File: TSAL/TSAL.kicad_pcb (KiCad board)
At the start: 2 copper layers, 100.2 x 100.2 mm, 65 parts, among them J1 Screw_Terminal_01x02, J2 Screw_Terminal_01x02, K1 RELAY_19.1x15.5mm, Q1 BC548, Q2 IRF3205, Q3 IRF3205, U1 MC34063AP, U2 TLP290-4, U3 LM555, U4 TL431DBZ, U5 TL431DBZ, U6 LM358

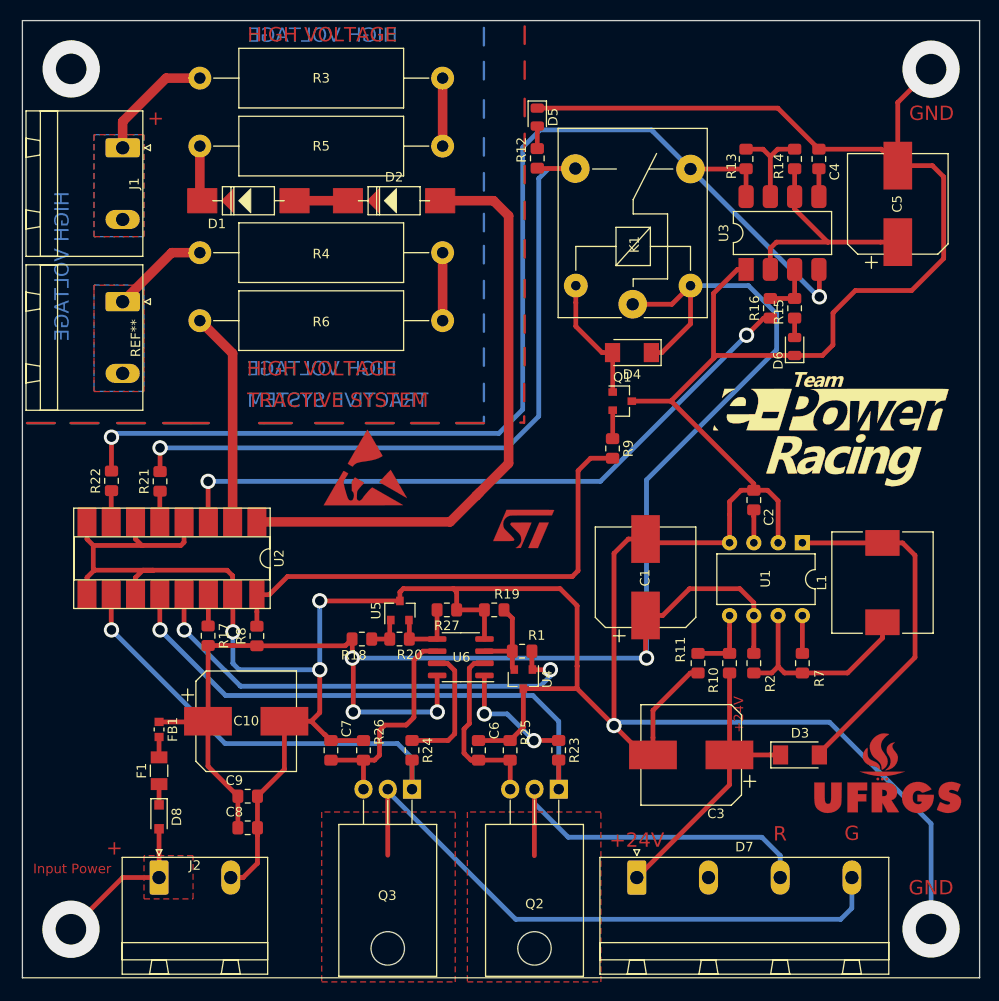
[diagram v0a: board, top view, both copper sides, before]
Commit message: TSAL rounded corners
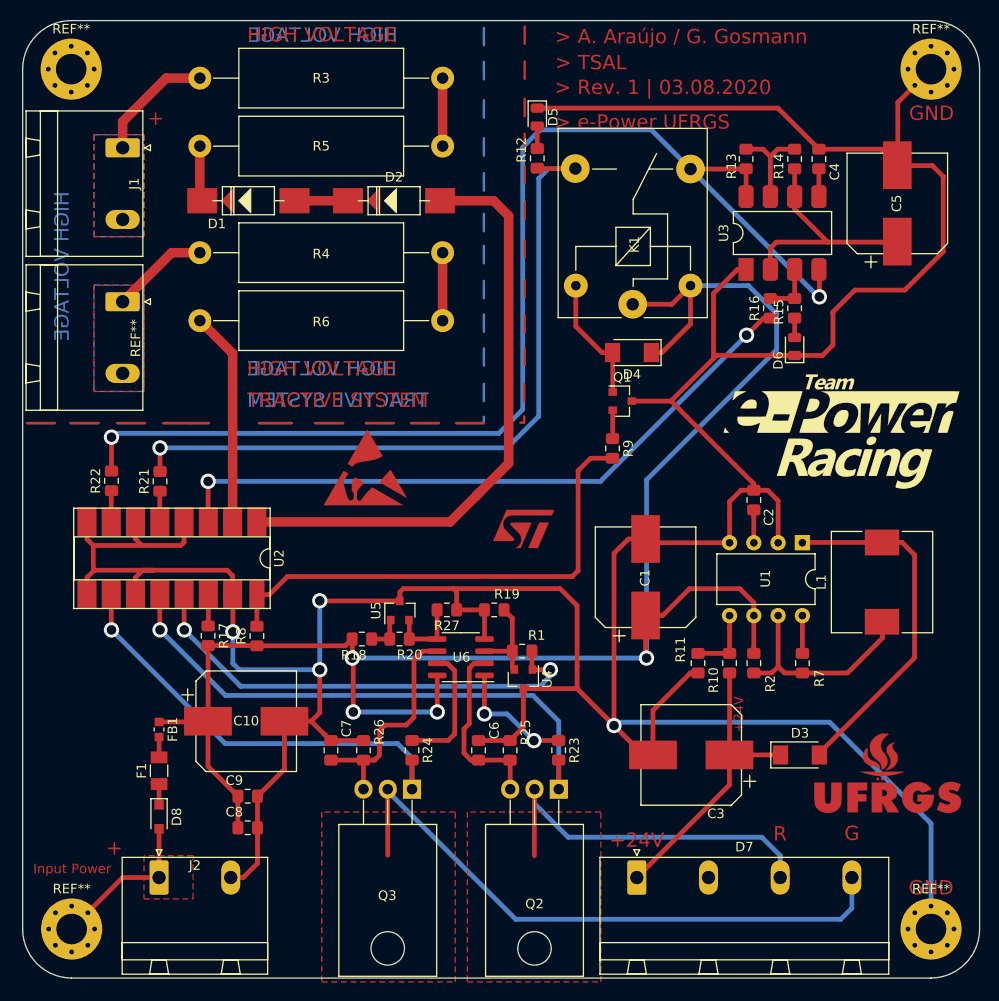
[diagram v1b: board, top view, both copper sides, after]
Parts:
- added REF**: MountingHole_3.2mm_M3_Pad_Via, e-Power:MountingHole_3.2mm_M3_Pad_Via, F.Cu at (133.9, 145.6)
- added REF**: MountingHole_3.2mm_M3_Pad_Via, e-Power:MountingHole_3.2mm_M3_Pad_Via, F.Cu at (223.8, 145.6)
- added REF**: MountingHole_3.2mm_M3_Pad_Via, e-Power:MountingHole_3.2mm_M3_Pad_Via, F.Cu at (223.8, 55.6)
- added REF**: MountingHole_3.2mm_M3_Pad_Via, e-Power:MountingHole_3.2mm_M3_Pad_Via, F.Cu at (133.8, 55.6)
- moved G*** 1.15 mm to (214.4, 93.5)
- moved C5 0.07 mm to (220.2, 69.7)
- moved L1 0.07 mm to (218.6, 109.3)
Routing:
- net GND: track 409.2 -> 408.8 mm, vias 6 -> 4
- net Input_Power: vias 1 -> 0
- net (no net): vias 1 -> 0
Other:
- board size 100.2 x 100.2 mm -> 100.1 x 100.2 mm
- board text added: "> A. Araújo / G. Gosmann"
- board text added: "> Rev. 1 | 03.08.2020"
- board text added: "> TSAL"
- board text added: "> e-Power UFRGS"

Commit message: update all circuits
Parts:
- removed the C1 at (193.9, 108.8)
- removed the C6 at (176.4, 126.9)
- removed the D3 at (210.1, 127.4)
- removed the D4 at (192.5, 85.3)
- removed G***: LOGO, e-Power:e-Power_22.8x12.0mm_Copper
- removed G***: LOGO, e-Power:ST_6.5x4.1mm_Copper
- removed G***: LOGO, e-Power:UFRGS_14.7x8.0mm_Copper
- removed the R10 at (202.7, 117.8)
- removed the R14 at (209.5, 65.0)
- removed REF** (x4): MountingHole_3.2mm_M3_Pad_Via, e-Power:MountingHole_3.2mm_M3_Pad_Via
- removed REF**: ESD-Logo_8.9x8mm_Copper, e-Power:ESD-Logo_8.9x8mm_Copper
- removed REF**: PhoenixContact_GMSTBA_2,5_2-G_1x02_P7.50mm_Horizontal, Connector_Phoenix_GMSTB:PhoenixContact_GMSTBA_2,5_2-G_1x02_P7.50mm_Horizontal
- removed the U4 at (181.1, 119.4)
- removed the U5 at (168.2, 112.3)
- added C11: 100nF, Capacitor_SMD:C_0805_2012Metric_Pad1.15x1.40mm_HandSolder, F.Cu at (183.7, 95.0)
- added C12: 100nF, Capacitor_SMD:C_0805_2012Metric_Pad1.15x1.40mm_HandSolder, F.Cu at (217.6, 86.2)
- added C13: 100nF, Capacitor_SMD:C_0805_2012Metric_Pad1.15x1.40mm_HandSolder, F.Cu at (220.6, 86.2)
- added C4: 100nF, Capacitor_SMD:C_0805_2012Metric_Pad1.15x1.40mm_HandSolder, F.Cu at (192.2, 87.8)
- added C5: 220u, e-Power:CP_Elec_10x10, F.Cu at (167.1, 92.3)
- added D2: SS54HF, e-Power:DO-214AC, F.Cu at (186.2, 88.4)
- added D7: SS54HF, e-Power:DO-214AC, F.Cu at (177.7, 94.9)
- added H1: MountingHole_Pad, e-Power:MountingHole_3.2mm_M3_Pad_Via, F.Cu at (134.3, 146.1)
- added H2: MountingHole_Pad, e-Power:MountingHole_3.2mm_M3_Pad_Via, F.Cu at (215.6, 130.7)
- added H3: MountingHole_Pad, e-Power:MountingHole_3.2mm_M3_Pad_Via, F.Cu at (223.5, 122.8)
- added H4: MountingHole_Pad, e-Power:MountingHole_3.2mm_M3_Pad_Via, F.Cu at (223.5, 130.7)
- added R12: 100K, Resistor_SMD:R_0805_2012Metric_Pad1.15x1.40mm_HandSolder, F.Cu at (181.3, 98.5)
- added R13: 100K, Resistor_SMD:R_0805_2012Metric_Pad1.15x1.40mm_HandSolder, F.Cu at (176.5, 98.5)
- added R17: 1R, Resistor_SMD:R_0805_2012Metric_Pad1.15x1.40mm_HandSolder, F.Cu at (185.0, 92.0)
- added R18: 10R, Resistor_SMD:R_0805_2012Metric_Pad1.15x1.40mm_HandSolder, F.Cu at (189.7, 92.0)
- added R19: 10R, Resistor_SMD:R_0805_2012Metric_Pad1.15x1.40mm_HandSolder, F.Cu at (176.5, 104.3)
- added R20: 10R, Resistor_SMD:R_0805_2012Metric_Pad1.15x1.40mm_HandSolder, F.Cu at (181.3, 101.4)
- added R24: 10K, Resistor_SMD:R_0805_2012Metric_Pad1.15x1.40mm_HandSolder, F.Cu at (196.9, 87.8)
- added R27: 10R, Resistor_SMD:R_0805_2012Metric_Pad1.15x1.40mm_HandSolder, F.Cu at (186.0, 97.9)
- added R28: 10R, Resistor_SMD:R_0805_2012Metric_Pad1.15x1.40mm_HandSolder, F.Cu at (194.5, 90.8)
- added R31: 10K, Resistor_SMD:R_0805_2012Metric_Pad1.15x1.40mm_HandSolder, F.Cu at (176.5, 101.4)
- added R32: 100K, Resistor_SMD:R_0805_2012Metric_Pad1.15x1.40mm_HandSolder, F.Cu at (186.0, 100.8)
- added R33: 10R, Resistor_SMD:R_0805_2012Metric_Pad1.15x1.40mm_HandSolder, F.Cu at (181.3, 107.3)
- added R34: 10R, Resistor_SMD:R_0805_2012Metric_Pad1.15x1.40mm_HandSolder, F.Cu at (194.5, 93.7)
- added R35: 10R, Resistor_SMD:R_0805_2012Metric_Pad1.15x1.40mm_HandSolder, F.Cu at (190.8, 97.9)
- added R39: 10R, Resistor_SMD:R_0805_2012Metric_Pad1.15x1.40mm_HandSolder, F.Cu at (199.2, 90.8)
- added R40: 10R, Resistor_SMD:R_0805_2012Metric_Pad1.15x1.40mm_HandSolder, F.Cu at (186.0, 103.8)
- added R41: 10R, Resistor_SMD:R_0805_2012Metric_Pad1.15x1.40mm_HandSolder, F.Cu at (190.8, 100.8)
- added R43: 10R, Resistor_SMD:R_0805_2012Metric_Pad1.15x1.40mm_HandSolder, F.Cu at (181.3, 104.3)
- added R44: 10R, Resistor_SMD:R_0805_2012Metric_Pad1.15x1.40mm_HandSolder, F.Cu at (186.0, 106.8)
- added R45: 10R, Resistor_SMD:R_0805_2012Metric_Pad1.15x1.40mm_HandSolder, F.Cu at (199.2, 93.7)
- added R46: 10R, Resistor_SMD:R_0805_2012Metric_Pad1.15x1.40mm_HandSolder, F.Cu at (195.5, 96.7)
- added R47: 10R, Resistor_SMD:R_0805_2012Metric_Pad1.15x1.40mm_HandSolder, F.Cu at (190.8, 103.8)
- added R48: 10R, Resistor_SMD:R_0805_2012Metric_Pad1.15x1.40mm_HandSolder, F.Cu at (195.5, 99.6)
- added R49: 10K, Resistor_SMD:R_0805_2012Metric_Pad1.15x1.40mm_HandSolder, F.Cu at (217.6, 81.4)
- added R50: 10K, Resistor_SMD:R_0805_2012Metric_Pad1.15x1.40mm_HandSolder, F.Cu at (223.5, 86.2)
- added TP1: 24V, e-Power:TestPoint_Pad_D1.0mm, F.Cu at (208.3, 129.0)
- added TP2: OUT, e-Power:TestPoint_Pad_D1.0mm, F.Cu at (217.7, 77.5)
- added TP3: Vref_R, e-Power:TestPoint_Pad_D1.0mm, F.Cu at (220.7, 77.8)
- added TP4: RS_R, e-Power:TestPoint_Pad_D1.0mm, F.Cu at (217.7, 74.5)
- added TP5: Vref_G, e-Power:TestPoint_Pad_D1.0mm, F.Cu at (200.8, 99.4)
- added TP6: RS_G, e-Power:TestPoint_Pad_D1.0mm, F.Cu at (220.7, 74.8)
- added TP7: 12V, e-Power:TestPoint_Pad_D1.0mm, F.Cu at (223.8, 74.8)
- added U2: NE555, Package_SO:SOIC-8_3.9x4.9mm_P1.27mm, F.Cu at (178.4, 89.6)
- added U6: TL431DBZ, Package_TO_SOT_SMD:SOT-23, F.Cu at (190.6, 107.5)
- C10: value 470u -> 220u
- C2: renamed from C5; footprint e-Power:CP_Elec_10x10 -> Capacitor_SMD:C_0805_2012Metric
- C3: value 100uF -> 220u
- C8: value 100n -> 100nF
- D4: renamed from D5; value LED -> LED GREEN; footprint LED_SMD:LED_0805_2012Metric -> LED_SMD:LED_0603_1608Metric
- D5: renamed from D6; value LED -> LED RED; footprint LED_SMD:LED_0805_2012Metric -> LED_SMD:LED_0603_1608Metric
- D8: value D_SCH_1N5819 -> SS54HF; footprint Diode_SMD:D_SOD-323_HandSoldering -> e-Power:DO-214AC
- J2: footprint Connector_Phoenix_GMSTB:PhoenixContact_GMSTBA_2,5_2-G_1x02_P7.50mm_Horizontal -> e-Power:TerminalBlock_Phoenix_MKDS-1,5-2_1x02_P5.08mm_Horizontal
- L1: value 170uH -> 100uH; footprint e-Power:L_10.4x10.4_H4.8 -> Inductor_SMD:L_12x12mm_H6mm
- Q1: value BC548 -> Si2302DS
- R14: renamed from R1; value 10K -> 1K
- R16: renamed from R19; value 10K -> ADJ
- R22: renamed from R2; value 0.68R -> 1R
- R25: value 22R -> 100K
- R26: value 27R -> 10R
- R30: renamed from R20; value 10K -> 1K
- R37: renamed from R27; value 10K -> ADJ
- U1: renamed from U2; footprint e-Power:TLP290-4 -> e-Power:SOIC-16_4.55x10.3mm_P1.27mm(TLP290-4)
- U3: value LM555 -> TL431DBZ; footprint Package_DIP:DIP-8_W7.62mm_LongPads -> Package_TO_SOT_SMD:SOT-23
- U5: renamed from U1; footprint Package_DIP:DIP-8_W7.62mm -> Package_SO:SO-8_3.9x4.9mm_P1.27mm
- moved F1 63.9 mm to (203.7, 109.2)
- moved R26 40.0 mm to (188.5, 95.0), turned to 0 degrees
- moved C3 39.2 mm to (167.1, 104.1), turned to 0 degrees
- moved Q1 31.2 mm to (221.4, 81.6), turned to 90 degrees
- moved U3 28.3 mm to (195.4, 103.4), turned to 0 degrees
- moved R25 19.9 mm to (176.5, 107.3), turned to 0 degrees
- moved U5 13.2 mm to (216.4, 93.5)
- moved J2 8.11 mm to (149.0, 145.6)
- renumbered C4 to C1, C2 to C6, D2 to D3, D7 to D6, R3 to R1, R17 to R10, R16 to R11, R23 to R15, R5 to R2, R7 to R23, R18 to R29, R8 to R3, R24 to R36, R11 to R38, R12 to R4, R22 to R42, R9 to R5, R4 to R6, R6 to R7, R13 to R8, R15 to R9, U6 to U4
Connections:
- C1 pad 2: Net-(C4-Pad2) -> Net-(C1-Pad2)
- C2 pad 1: Net-(C5-Pad1) -> Net-(C2-Pad1)
- J1 pad 1: Net-(J1-Pad2) -> Net-(J1-Pad1)
- K1 pad 5: Net-(D4-Pad2) (its old number) -> Net-(D2-Pad2)
- Q1 pad 1: Net-(D4-Pad2) (its old number) -> Net-(Q1-Pad1)
- Q1 pad 2: Net-(Q1-Pad2) -> GND
- Q1 pad 3: GND -> Net-(D2-Pad2)
- Q2 pad 3: Net-(C6-Pad2) (its old number) -> Net-(C4-Pad2)
- R11 pad 2: Net-(R15-Pad2) -> Net-(R11-Pad2)
- R14 pad 1: Net-(R1-Pad1) (its old number) -> Net-(R14-Pad1)
- R14 pad 2: Net-(R1-Pad2) -> Net-(R14-Pad2)
- R16 pad 2: Net-(R1-Pad1) (its old number) -> Net-(R14-Pad1)
- R25 pad 1: GND -> +24V
- R25 pad 2: Net-(C6-Pad2) (its old number) -> Net-(R25-Pad2)
- R26 pad 1: GND -> Net-(R26-Pad1)
- R26 pad 2: Net-(C7-Pad2) -> Net-(R18-Pad1)
- R5 pad 1: Net-(Q1-Pad2) -> Net-(Q1-Pad1)
- R8 pad 2: Net-(R13-Pad2) -> Net-(R12-Pad2)
- R9 pad 2: Net-(R15-Pad2) -> Net-(R11-Pad2)
- U1 pad 13: Net-(R1-Pad2) -> Net-(R14-Pad2)
- U3 pad 1: GND -> Net-(R14-Pad2)
- U3 pad 2: Net-(C5-Pad1) -> Net-(R14-Pad1)
- U3 pad 3: Net-(R15-Pad2) -> GND
- U4 pad 2: Net-(C6-Pad2) (its old number) -> Net-(C12-Pad1)
- U4 pad 3: Net-(R1-Pad1) (its old number) -> Net-(R14-Pad1)
- U4 pad 6: Net-(C7-Pad2) -> Net-(C13-Pad1)
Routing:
- net Net-(R1-Pad2): track 49.4 -> 0.00 mm, vias 2 -> 0
- net Net-(R14-Pad2): track 0.00 -> 49.0 mm, vias 0 -> 2
- net Net-(C6-Pad2) (its old number): track 19.1 -> 0.00 mm
- net Net-(C4-Pad2): track 2.91 -> 19.1 mm
- net Net-(D4-Pad2) (its old number): track 13.4 -> 0.00 mm
- net Net-(D2-Pad2): track 0.00 -> 13.4 mm
- net (no net): track 98.7 -> 88.2 mm, vias 0 -> 2
- net Net-(R13-Pad2): track 9.91 -> 0.00 mm
- net Net-(R12-Pad2): track 0.00 -> 9.91 mm
- net Net-(R14-Pad1): track 0.00 -> 9.60 mm
- net Net-(R1-Pad1) (its old number): track 9.60 -> 0.00 mm
- net +12V: track 183.0 -> 189.2 mm
- net Net-(R15-Pad2): track 5.58 -> 0.00 mm
- net Net-(R11-Pad2): track 0.00 -> 5.58 mm
- net Net-(Q1-Pad2): track 2.98 -> 0.00 mm
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- added copper zone on F.Cu, net Net-(D7-Pad3)
- added copper zone on F.Cu, net Net-(D7-Pad4)
- removed copper zone on F.Cu, net Net-(D6-Pad3)
- removed copper zone on F.Cu, net Net-(D6-Pad4)
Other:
- board size 100.1 x 100.2 mm -> 100.1 x 100.1 mm
- board text added: "> Rev. A | 03.08.2020"
- board text removed: "> Rev. 1 | 03.08.2020"

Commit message: update tsal
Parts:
- moved U1 10.2 mm to (154.1, 92.8)
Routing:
- net Net-(D3-Pad2): track 62.9 -> 7.56 mm
- net Net-(R7-Pad1): track 22.5 -> 4.85 mm
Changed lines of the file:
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@@
     (thickness 1.6)
     (drawings 36)
-    (tracks 421)
+    (tracks 415)
     (zones 0)
     (modules 97)
@@
   )
   (module "e-Power:SOIC-16_4.55x10.3mm_P1.27mm(TLP290-4)" (layer F.Cu)
-    (at 153.2382 102.997 270)
+    (at 154.10942 92.79636 270)
     (descr "SOIC, 16 Pin (https://toshiba.semicon-storage.com/info/docget.jsp?did=12858&prodName=TLP291-4), generated with kicad-footprint-generator ipc_gullwing_generator.py")
     (tags "SOIC SO")
@@
   (segment (start 190.4652 85.2965) (end 190.4492 85.2805) (width 0.5) (layer F.Cu) (net 3))
   (segment (start 190.4652 89.4105) (end 190.4652 85.2965) (width 0.5) (layer F.Cu) (net 3))
-  (segment (start 173.4566 102.997) (end 153.2382 102.997) (width 1) (layer F.Cu) (net 4))
   (segment (start 172.6692 69.3928) (end 178.0032 69.3928) (width 1) (layer F.Cu) (net 4))
   (segment (start 178.0032 69.3928) (end 179.578 70.9676) (width 1) (layer F.Cu) (net 4))
-  (segment (start 179.578 96.8756) (end 176.1744 100.2792) (width 1) (layer F.Cu) (net 4))
-  (segment (start 179.578 70.9676) (end 179.578 96.8756) (width 1) (layer F.Cu) (net 4))
-  (segment (start 176.5808 99.8728) (end 176.1744 100.2792) (width 1) (layer F.Cu) (net 4))
-  (segment (start 176.1744 100.2792) (end 173.4566 102.997) (width 1) (layer F.Cu) (net 4))
   (segment (start 202.692 127.3678) (end 202.6788 127.381) (width 0.5) (layer F.Cu) (net 5))
   (segment (start 202.692 118.8048) (end 202.692 127.3678) (width 0.5) (layer F.Cu) (net 5))
@@
   (segment (start 207.1026 118.8048) (end 205.232 118.8048) (width 0.5) (layer F.Cu) (net 18))
   (segment (start 207.772 118.1354) (end 207.1026 118.8048) (width 0.5) (layer F.Cu) (net 18))
-  (segment (start 150.6982 85.3694) (end 150.6982 102.997) (width 1) (layer F.Cu) (net 19))
   (segment (start 147.2692 81.9404) (end 150.6982 85.3694) (width 1) (layer F.Cu) (net 19))
   (segment (start 143.0782 99.8056) (end 143.1036 99.7802) (width 0.5) (layer F.Cu) (net 21))
@@
   (segment (start 179.9627 113.0755) (end 179.0917 112.2045) (width 0.5) (layer F.Cu) (net 46))
   (segment (start 179.9627 116.5225) (end 179.9627 113.0755) (width 0.5) (layer F.Cu) (net 46))
-  (via (at 182.2196 125.8824) (size 1.6) (drill 1) (layers F.Cu B.Cu) (net 56))
-  (segment (start 184.8104 125.8644) (end 182.2376 125.8644) (width 0.5) (layer F.Cu) (net 56))
-  (segment (start 182.2376 125.8644) (end 182.2196 125.8824) (width 0.5) (layer F.Cu) (net 56))
-  (via (at 177.038 123.0884) (size 1.6) (drill 1) (layers F.Cu B.Cu) (net 56))
-  (segment (start 182.2196 125.8824) (end 179.4256 123.0884) (width 0.5) (layer B.Cu) (net 56))
-  (segment (start 179.4256 123.0884) (end 177.038 123.0884) (width 0.5) (layer B.Cu) (net 56))
-  (segment (start 177.038 119.0737) (end 177.0492 119.0625) (width 0.5) (layer F.Cu) (net 56))
-  (segment (start 177.038 123.0884) (end 177.038 119.0737) (width 0.5) (layer F.Cu) (net 56))
   (segment (start 167.1357 115.2525) (end 165.2487 115.2525) (width 0.5) (layer F.Cu) (net 50))
   (segment (start 167.1357 113.3811) (end 167.2488 113.268) (width 0.5) (layer F.Cu) (net 50))
@@
   (segment (start 202.692 112.8014) (end 202.692 114.1514) (width 0.5) (layer F.Cu) (net 52))
   (segment (start 202.692 116.7548) (end 199.39 116.7548) (width 0.5) (layer F.Cu) (net 52))
+  (segment (start 137.9982 99.7548) (end 138.0236 99.7294) (width 0.5) (layer F.Cu) (net 54))
+  (segment (start 137.9982 102.997) (end 137.9982 99.7548) (width 0.5) (layer F.Cu) (net 54))
+  (via (at 182.2196 125.8824) (size 1.6) (drill 1) (layers F.Cu B.Cu) (net 56))
+  (segment (start 184.8104 125.8644) (end 182.2376 125.8644) (width 0.5) (layer F.Cu) (net 56))
+  (segment (start 182.2376 125.8644) (end 182.2196 125.8824) (width 0.5) (layer F.Cu) (net 56))
+  (via (at 177.038 123.0884) (size 1.6) (drill 1) (layers F.Cu B.Cu) (net 56))
+  (segment (start 182.2196 125.8824) (end 179.4256 123.0884) (width 0.5) (layer B.Cu) (net 56))
+  (segment (start 179.4256 123.0884) (end 177.038 123.0884) (width 0.5) (layer B.Cu) (net 56))
+  (segment (start 177.038 119.0737) (end 177.0492 119.0625) (width 0.5) (layer F.Cu) (net 56))
+  (segment (start 177.038 123.0884) (end 177.038 119.0737) (width 0.5) (layer F.Cu) (net 56))
   (segment (start 173.1742 117.7925) (end 172.0992 117.7925) (width 0.5) (layer F.Cu) (net 58))
   (segment (start 173.9392 118.5575) (end 173.1742 117.7925) (width 0.5) (layer F.Cu) (net 58))
@@
   (segment (start 169.4688 125.8644) (end 173.246 125.8644) (width 0.5) (layer F.Cu) (net 58))
   (segment (start 173.246 125.8644) (end 173.9392 125.1712) (width 0.5) (layer F.Cu) (net 58))
-  (segment (start 137.9982 99.7548) (end 138.0236 99.7294) (width 0.5) (layer F.Cu) (net 54))
-  (segment (start 137.9982 102.997) (end 137.9982 99.7548) (width 0.5) (layer F.Cu) (net 54))
   (zone (net 15) (net_name "Net-(D7-Pad4)") (layer F.Cu) (hatch edge 0.508)
     (connect_pads (clearance 0.508))

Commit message: review das placas
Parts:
- added TP10: GND, e-Power:TestPoint_Pad_D1.0mm, F.Cu at (154.1, 146.4)
- added TP8: G, e-Power:TestPoint_Pad_D1.0mm, F.Cu at (217.1, 113.4)
- added TP9: 1.25V, e-Power:TestPoint_Pad_D1.0mm, F.Cu at (156.8, 146.4)
- C10, C3, C5: value 220u -> 220uF
- D6: footprint Connector_Phoenix_GMSTB:PhoenixContact_GMSTBA_2,5_4-G_1x04_P7.50mm_Horizontal -> e-Power:TerminalBlock_Phoenix_MKDS-1,5-4-5.08_1x04_P5.08mm_Horizontal
- H1: value MountingHole_Pad -> +12V
- H2, H3, H4: value MountingHole_Pad -> GND
- J1: footprint Connector_Phoenix_GMSTB:PhoenixContact_GMSTBA_2,5_2-G_1x02_P7.50mm_Horizontal -> e-Power:TerminalBlock_Phoenix_MKDS-1,5-2_1x02_P5.08mm_Horizontal
- Q2, Q3: footprint Package_TO_SOT_THT:TO-220-3_Horizontal_TabDown -> e-Power:TO-220-3_Horizontal_TabDown
- U5: value MC34063AP -> MC34063; footprint Package_SO:SO-8_3.9x4.9mm_P1.27mm -> Package_SO:SOIC-8_3.9x4.9mm_P1.27mm
- moved H4 117.0 mm to (133.8, 55.7)
- moved C1 112.0 mm to (188.7, 174.6)
- moved R8 105.3 mm to (178.0, 167.0)
- moved C2 104.2 mm to (189.4, 169.3)
- moved TP2 98.8 mm to (198.1, 174.3)
- moved R11 98.3 mm to (196.8, 178.4)
- moved TP7 96.2 mm to (159.4, 146.4)
- moved R9 95.1 mm to (195.0, 174.6)
- moved F1 94.5 mm to (133.8, 172.8), turned to 270 degrees
- moved R39 94.1 mm to (253.4, 167.7)
- moved C11 89.7 mm to (248.9, 156.6)
- moved R41 88.2 mm to (252.9, 163.4)
- moved R40 86.2 mm to (247.8, 163.9)
- moved R43 85.8 mm to (243.3, 163.7)
- moved R47 85.7 mm to (251.1, 164.7)
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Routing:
- net GND: track 411.7 -> 54.9 mm, vias 4 -> 0
- net +12V: track 189.2 -> 57.6 mm, vias 4 -> 0
- net Net-(K1-Pad3): track 125.9 -> 40.7 mm, vias 2 -> 1
- net Net-(R11-Pad1): track 70.2 -> 0.00 mm, vias 2 -> 1
- net Net-(Q2-Pad1): track 59.5 -> 0.00 mm, vias 1 -> 0
- net Net-(R31-Pad2): track 7.26 -> 64.4 mm
- net Net-(R3-Pad2): track 52.5 -> 1.49 mm
- net Net-(R14-Pad2): track 49.0 -> 0.00 mm, vias 2 -> 0
- net Net-(Q3-Pad1): track 47.0 -> 0.00 mm, vias 1 -> 0
- net Net-(K1-Pad4): track 76.6 -> 36.3 mm
- net Net-(D6-Pad3): track 38.7 -> 0.00 mm
- net Net-(C5-Pad1): track 24.9 -> 0.00 mm
- net Net-(C7-Pad2): track 23.9 -> 0.00 mm
- net Net-(D7-Pad2): track 37.4 -> 15.9 mm
- net Net-(C4-Pad2): track 19.1 -> 0.00 mm
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- removed copper zone on F.Cu, net Input_Power
- removed copper zone on F.Cu, net Net-(D7-Pad3)
- removed copper zone on F.Cu, net Net-(D7-Pad4)
- removed copper zone on B.Cu, net Net-(J1-Pad1)
- removed copper zone on F.Cu, net Net-(J1-Pad1)
- removed copper zone on B.Cu, net Net-(J1-Pad2)
- removed copper zone on F.Cu, net Net-(J1-Pad2)
